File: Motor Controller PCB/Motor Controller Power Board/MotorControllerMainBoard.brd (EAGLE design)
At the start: 60 x 118 mm, 52 parts, among them U1 CDBA340L-G

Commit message: shrunk board size to 10x6cm
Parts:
- removed U$10, U$20: EEU-FM1H102B, MotorControllerEagleLibrary:EEU-FM1H102B
- C36, C37, C38, C39, C40: value (none) -> 22uF; device resistor:C1206 -> rcl:C1210
- moved C38 77.4 mm to (17.0, 35.5), flipped to the bottom
- moved C37 75.4 mm to (12.0, 37.0), flipped to the bottom, turned to 180 degrees
- moved C39 64.5 mm to (12.0, 49.0), flipped to the bottom, turned to 180 degrees
- moved C1 61.3 mm to (31.0, 74.0), turned to 0 degrees
- moved C36 48.1 mm to (12.0, 41.0), flipped to the bottom
- moved U$19 34.3 mm to (44.1, 40.0), flipped to the bottom, turned to 270 degrees
- moved U$18 31.8 mm to (53.0, 40.0), turned to 270 degrees
- moved U$13 31.1 mm to (35.3, 40.0), flipped to the top, turned to 270 degrees
- moved C40 24.2 mm to (12.0, 45.0), flipped to the bottom, turned to 180 degrees
- moved SV8 16.0 mm to (57.0, 26.7)
- moved C19 10.5 mm to (28.7, 44.1), flipped to the bottom
- moved SV9 10.3 mm to (48.3, 23.1), turned to 180 degrees
- moved U$22 9.43 mm to (40.0, 28.0)
- moved 3.3_CONFIRM 8.60 mm to (40.1, 30.1)
- moved L1 8.04 mm to (25.7, 39.4)
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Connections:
- net GND: no longer U$10.NEGATIVE, U$20.NEGATIVE
- net INPUT_POWER(+): no longer U$10.POSITIVE, U$20.POSITIVE
- net MOTOR_OUTPUT_(+): now also U$9.PIN4; no longer U$9.PIN5
- net POWER_INPUT(+): now also U$9.PIN5; no longer U$9.PIN4
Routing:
- net INPUT_POWER(+): track 0.00 -> 50.2 mm
- net 3.3V_ISOLATED: track 0.00 -> 35.8 mm
- net GND_ISOLATED: track 0.00 -> 29.3 mm, vias 0 -> 2
- net CURRENT_SENSOR_OUTPUT: track 0.00 -> 29.2 mm
- net N$17: track 0.00 -> 4.78 mm
- net GND: track 0.00 -> 3.66 mm
- net N$14: track 0.00 -> 2.27 mm
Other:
- board size 60 x 118 mm -> 60 x 100 mm

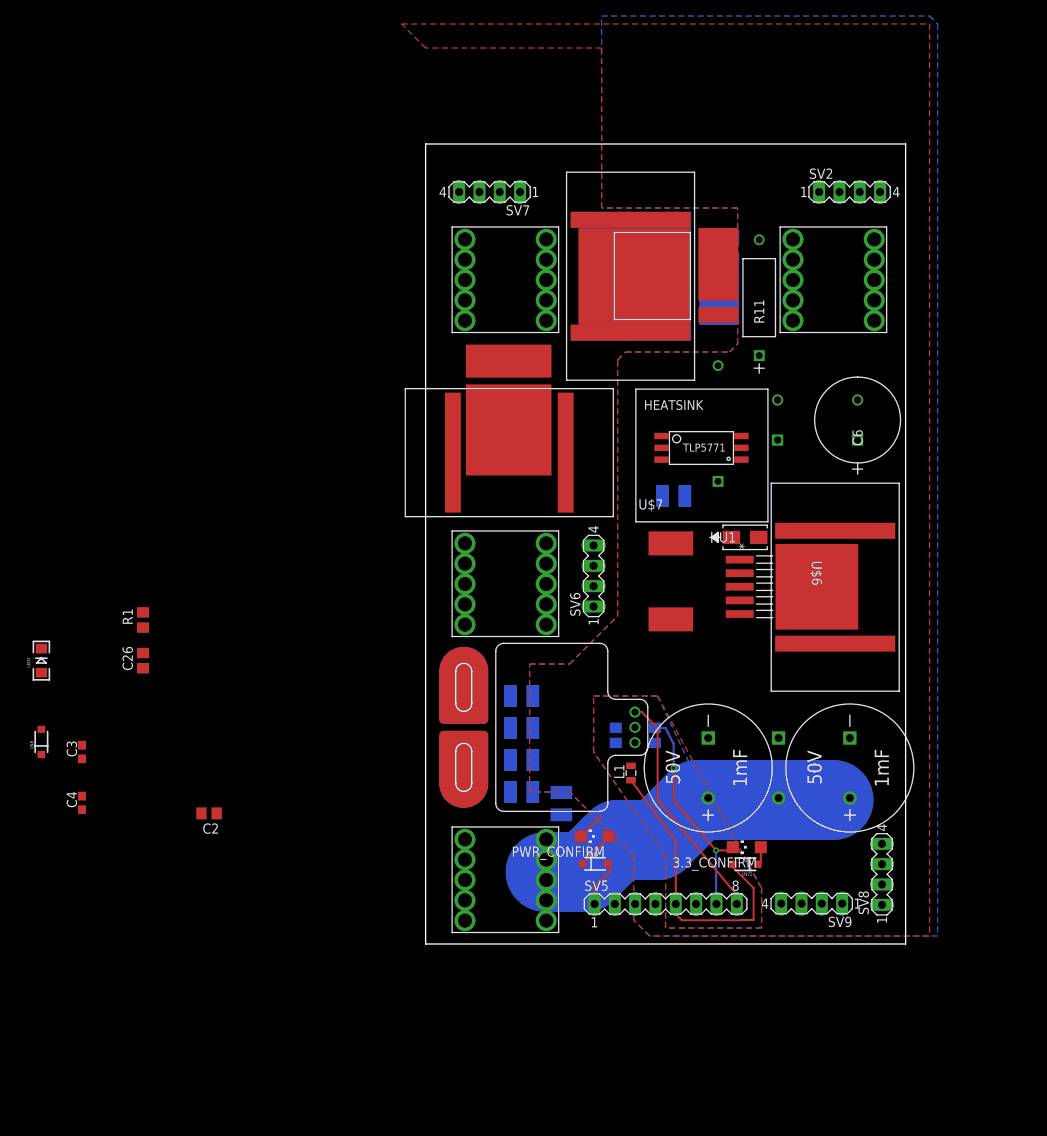
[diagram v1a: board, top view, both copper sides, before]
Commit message: Changed connections to logic board
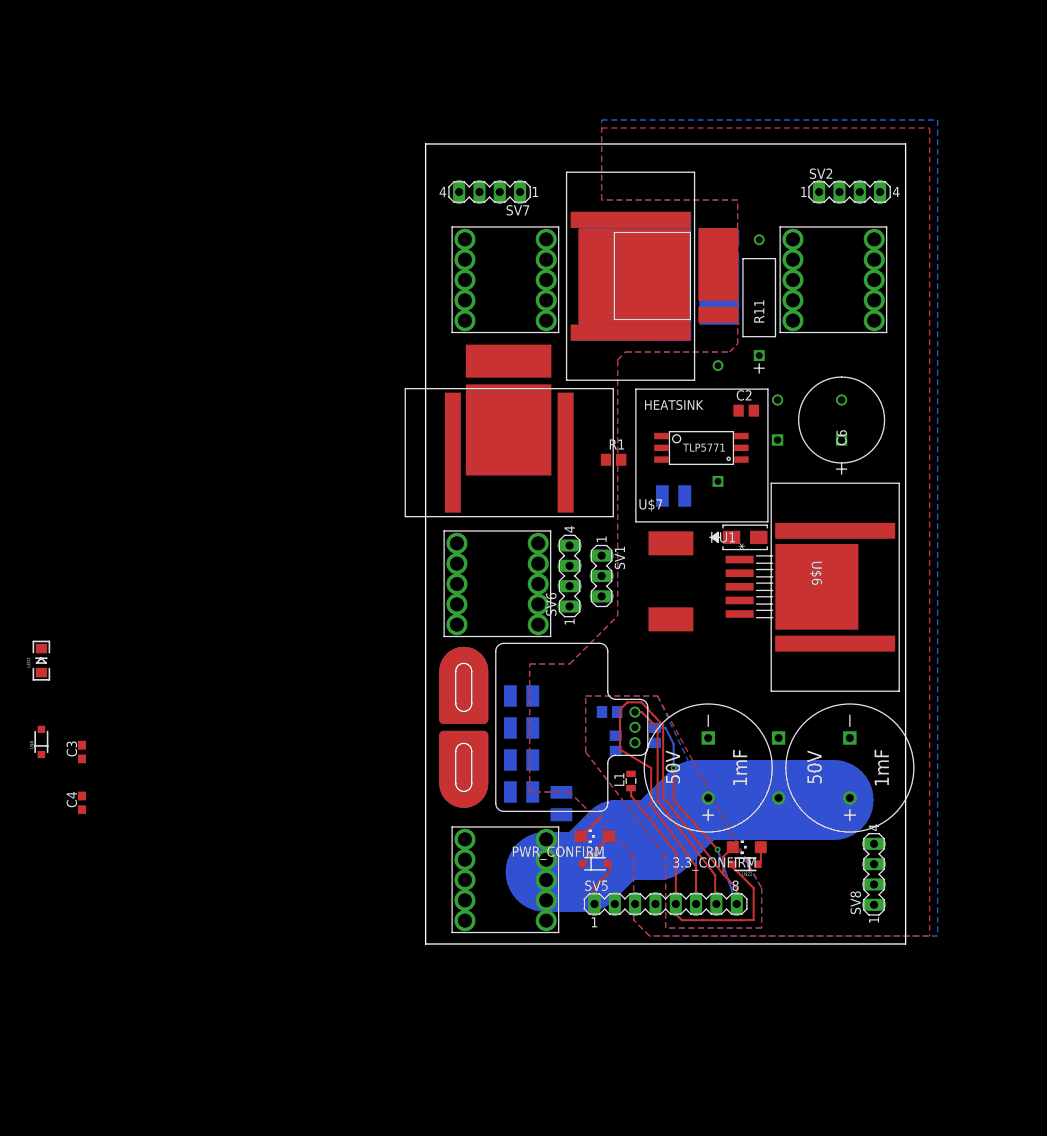
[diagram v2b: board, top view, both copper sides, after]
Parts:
- removed SV9: (no value), con-lstb:MA04-1
- added SV1: (no value), con-lstb:MA03-1
- moved C2 83.9 mm to (40.1, 84.7), turned to 0 degrees
- moved R1 62.1 mm to (23.5, 78.5), turned to 0 degrees
- moved C26 58.7 mm to (23.0, 47.0), flipped to the bottom, turned to 0 degrees
- moved SV6 3.00 mm to (18.0, 64.0)
- moved C6 2.00 mm to (52.0, 86.0)
- moved C20 1.00 mm to (23.8, 43.1)
- moved L1 1.00 mm to (25.7, 38.4)
- moved SV8 1.00 mm to (56.0, 26.7)
- moved U$15 1.00 mm to (9.00, 63.0)
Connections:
- net 3.3V_ISOLATED: now also SV1.1, SV6.1; no longer SV9.1
- net CURRENT_SENSOR_OUTPUT: now also SV5.7; no longer SV5.8, SV9.3
- net GND_ISOLATED: now also SV1.3, SV5.6, SV5.8, SV6.2, SV6.4; no longer SV5.7, SV9.4
- net TEENSY_FET_DRIVER_SIGNAL: now also SV1.2, SV6.3; no longer SV5.6, SV9.2
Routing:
- net GND_ISOLATED: track 29.3 -> 103.3 mm
- net INPUT_POWER(+): track 50.2 -> 54.8 mm
- net CURRENT_SENSOR_OUTPUT: track 29.2 -> 28.2 mm
- net 3.3V_ISOLATED: track 35.8 -> 34.9 mm

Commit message: this is going to be nuked when i change headers
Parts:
- added SV3: (no value), con-lstb:MA04-1
- added U$10: EEU-FM1H102B, MotorControllerEagleLibrary:EEU-FM1H102B
- moved U$11 53.6 mm to (73.2, 15.0)
- moved PWR_CONFIRM 53.4 mm to (73.2, 19.4)
- moved SV8 46.5 mm to (51.4, 73.0), turned to 0 degrees
- moved 3.3_CONFIRM 33.1 mm to (69.2, 14.1)
- moved U$13 32.9 mm to (24.3, 9.00)
- moved U$18 32.9 mm to (42.0, 9.00)
- moved U$19 32.9 mm to (33.1, 9.00)
- moved U$22 32.8 mm to (68.0, 11.0)
- moved U$12 18.0 mm to (9.00, 8.00)
- moved U$25 18.0 mm to (25.3, 52.8)
- moved U$17 18.0 mm to (38.6, 60.1)
- moved C1 18.0 mm to (31.0, 56.0)
- moved C19 18.0 mm to (28.7, 26.1)
- moved C2 18.0 mm to (40.1, 66.7)
- moved C20 18.0 mm to (23.8, 25.1)
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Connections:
- net GND: now also U$10.NEGATIVE
- net INPUT_POWER(+): now also U$10.POSITIVE
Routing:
- net GND_ISOLATED: track 103.3 -> 0.00 mm, vias 2 -> 0
- net INPUT_POWER(+): track 54.8 -> 0.00 mm
- net 3.3V_ISOLATED: track 34.9 -> 0.00 mm
- net CURRENT_SENSOR_OUTPUT: track 28.2 -> 0.00 mm
- net N$17: track 4.78 -> 0.00 mm
- net GND: track 3.66 -> 0.00 mm
- net N$14: track 2.27 -> 0.00 mm
- removed copper zone on layer 1, net N$3
- removed copper zone on layer 16, net N$5

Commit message: Made a layout, need labels
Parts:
- removed C5, C6: EEUFR1H221B, MotorControllerEagleLibrary:CAP_PAN_10X16
- removed SV2, SV3, SV6, SV7: (no value), con-lstb:MA04-1
- removed SV5: (no value), con-lstb:MA08-1
- removed U$24: DA-T263-101E, MotorControllerEagleLibrary:DA-T263-101E
- removed U$7: 100uH, MotorControllerEagleLibrary:INDUCTOR_SMD_FOOTPRINT
- removed U1: CDBA340L-G, MotorControllerEagleLibrary:CDBA-G
- added J1: (no value), SparkFun-Connectors:DB9
- 3.3_CONFIRM, PWR_CONFIRM: device led:CHIPLED_1206 -> SparkFun-LED:LED-1206
- U$12, U$14, U$15, U$16: value 732-3204-ND_CONNECTOR -> 74650073R; device Connector 732-3204:732-3204-ND -> MotorControllerEagleLibrary:74650073R
- U$6: value TL2575HV-15IKTTR -> KHHD004A2B; device MotorControllerEagleLibrary:KTT5_6P22X6P86 -> MotorControllerEagleLibrary:KHHD004A2B
- moved C4 108.9 mm to (60.0, 71.0), turned to 0 degrees
- moved C3 105.6 mm to (58.0, 73.1), turned to 0 degrees
- moved LED2 100.6 mm to (52.0, 43.0)
- moved U$8 97.0 mm to (49.0, 42.0)
- moved U$12 82.0 mm to (7.00, 90.0), turned to 0 degrees
- moved U$15 61.7 mm to (56.0, 85.0)
- moved U$16 60.1 mm to (6.00, 23.0), turned to 0 degrees
- moved U$14 53.3 mm to (5.00, 56.0), turned to 0 degrees
- moved U$11 45.1 mm to (37.0, 42.0), turned to 90 degrees
- moved PWR_CONFIRM 40.7 mm to (40.0, 43.0)
- moved U$22 39.9 mm to (43.0, 42.0), turned to 90 degrees
- moved 3.3_CONFIRM 37.0 mm to (46.0, 43.0)
- moved C38 32.7 mm to (49.0, 11.0), turned to 270 degrees
- moved U$6 32.0 mm to (21.0, 29.0), flipped to the bottom, turned to 90 degrees
- moved C40 31.4 mm to (39.0, 11.0), turned to 270 degrees
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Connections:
- removed net N$1: U$6.2, U$7.1, U1.1
- removed net POWER_INPUT(+): U$9.PIN5
- new net ENABLE_12V: J1.8, U$6.ON/OFF
- new net N$11: U$6.SENSE+
- new net N$5: U$6.SENSE-
- new net N$8: U$6.TRIM
- net 12V_POWER_REGULATED: now also J1.2, U$6.VO+; no longer C5.1, C6.1, U$6.4, U$7.2
- net 3.3V_ISOLATED: now also J1.1, J1.9; no longer SV5.5, SV6.1
- net CURRENT_SENSOR_OUTPUT: now also J1.5; no longer SV5.7
- net GND: now also J1.7, U$15.P$1, U$15.P$2, U$15.P$3, U$15.P$4, U$6.VI-, U$6.VO-; no longer C5.2, C6.2, SV5.3, SV5.4, U$14.P$1, U$14.P$10, U$14.P$2, U$14.P$3, U$14.P$4, U$14.P$5, U$14.P$6, U$14.P$7, U$14.P$8, U$14.P$9, U$24.GND, U$24.GND2\, U$6.3, U$6.5, U$6.6, U1.2
- net GND_ISOLATED: now also J1.4; no longer SV5.6, SV5.8, SV6.2, SV6.4
- net INPUT_POWER(+): now also J1.3, U$14.P$1, U$14.P$2, U$14.P$3, U$14.P$4, U$6.VI+, U$9.PIN4; no longer C36.1, C37.1, C38.1, C39.1, C40.1, SV5.1, SV5.2, U$10.POSITIVE, U$12.P$1, U$12.P$10, U$12.P$2, U$12.P$3, U$12.P$4, U$12.P$5, U$12.P$6, U$12.P$7, U$12.P$8, U$12.P$9, U$13.POSITIVE, U$18.POSITIVE, U$19.POSITIVE
- net MOTOR_OUTPUT_(+): now also C36.1, C37.1, C38.1, C39.1, C40.1, U$10.POSITIVE, U$13.POSITIVE, U$16.P$1, U$16.P$2, U$16.P$3, U$16.P$4, U$18.POSITIVE, U$19.POSITIVE, U$9.PIN5; no longer U$15.P$1, U$15.P$10, U$15.P$2, U$15.P$3, U$15.P$4, U$15.P$5, U$15.P$6, U$15.P$7, U$15.P$8, U$15.P$9, U$6.1, U$9.PIN4
- net MOTOR_OUTPUT_(--): now also U$12.P$1, U$12.P$2, U$12.P$3, U$12.P$4; no longer U$16.P$1, U$16.P$10, U$16.P$2, U$16.P$3, U$16.P$4, U$16.P$5, U$16.P$6, U$16.P$7, U$16.P$8, U$16.P$9
- net TEENSY_FET_DRIVER_SIGNAL: now also J1.6, U$17.1.ANODE; no longer SV6.3
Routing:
- net INPUT_POWER(+): track 0.00 -> 131.8 mm, vias 0 -> 2
- net 12V_POWER_REGULATED: track 0.00 -> 103.0 mm, vias 0 -> 2
- net GND_ISOLATED: track 0.00 -> 97.9 mm, vias 0 -> 1
- net MOTOR_OUTPUT_(+): track 0.00 -> 72.1 mm
- net 3.3V_ISOLATED: track 0.00 -> 62.4 mm, vias 0 -> 2
- net GND: track 0.00 -> 56.9 mm, vias 0 -> 22
- net ENABLE_12V: track 0.00 -> 55.5 mm
- net FET_DRIVER_SIGNAL: track 0.00 -> 50.3 mm
- net CURRENT_SENSOR_OUTPUT: track 0.00 -> 39.4 mm
- net TEENSY_FET_DRIVER_SIGNAL: track 0.00 -> 35.8 mm
- net N$10: track 0.00 -> 17.4 mm
- net N$7: track 0.00 -> 12.8 mm
- net N$2: track 0.00 -> 9.98 mm
- net N$6: track 0.00 -> 8.52 mm
- net N$14: track 0.00 -> 3.47 mm
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- added copper zone on layer 1, net INPUT_POWER(+)
- added copper zone on layer 16, net INPUT_POWER(+)
- added copper zone on layer 1, net MOTOR_OUTPUT_(+)
- added copper zone on layer 16, net MOTOR_OUTPUT_(+)
- added copper zone on layer 1, net MOTOR_OUTPUT_(--)
- added copper zone on layer 16, net MOTOR_OUTPUT_(--)
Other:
- board size 60 x 100 mm -> 70 x 100 mm

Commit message: added TVS diodes and text
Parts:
- removed SV8: (no value), con-lstb:MA04-1
- added SV2: (no value), con-lstb:MA03-1
- added U$20, U$7: SMBJ15CD, MotorControllerEagleLibrary:SMB-DIODE
- added U$21, U$24: SS110-TP, MotorControllerEagleLibrary:SMA-DIODE
- moved U$12 7.00 mm to (14.0, 90.0)
- moved U$16 1.41 mm to (5.00, 24.0)
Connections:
- new net N$1: U$24.A, U$7.A
- new net N$4: U$20.A, U$21.A
- net 12V_POWER_REGULATED: now also SV2.1; no longer SV8.2
- net FET_DRIVER_SIGNAL: now also SV2.2; no longer SV8.3
- net GND: now also SV2.3, U$21.C, U$24.C; no longer SV8.4
- net MOTOR_OUTPUT_(+): no longer SV8.1
- net N$10: now also U$20.C
- net N$2: now also U$7.C
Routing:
- net MOTOR_OUTPUT_(+): track 72.1 -> 0.00 mm
- net 3.3V_ISOLATED: track 62.4 -> 78.8 mm, vias 2 -> 3
- net N$10: track 17.4 -> 23.9 mm
- net N$4: track 0.00 -> 5.69 mm
- net N$2: track 9.98 -> 15.6 mm
- net N$1: track 0.00 -> 4.18 mm
- net INPUT_POWER(+): track 131.8 -> 132.5 mm
- net GND: vias 22 -> 21
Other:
- board text added: "12V"
- board text added: "12V_ON"
- board text added: "3.3V_ISO"
- board text added: "3.3V_ON"
- board text added: "DRVR_SIG"
- board text added: "GND"
- board text added: "GND_ISO"
- board text added: "M+"
- board text added: "M-"
- board text added: "PWR_ON"
- board text added: "TNZY_FET_DRVR"
- board text removed: "Logic Board"

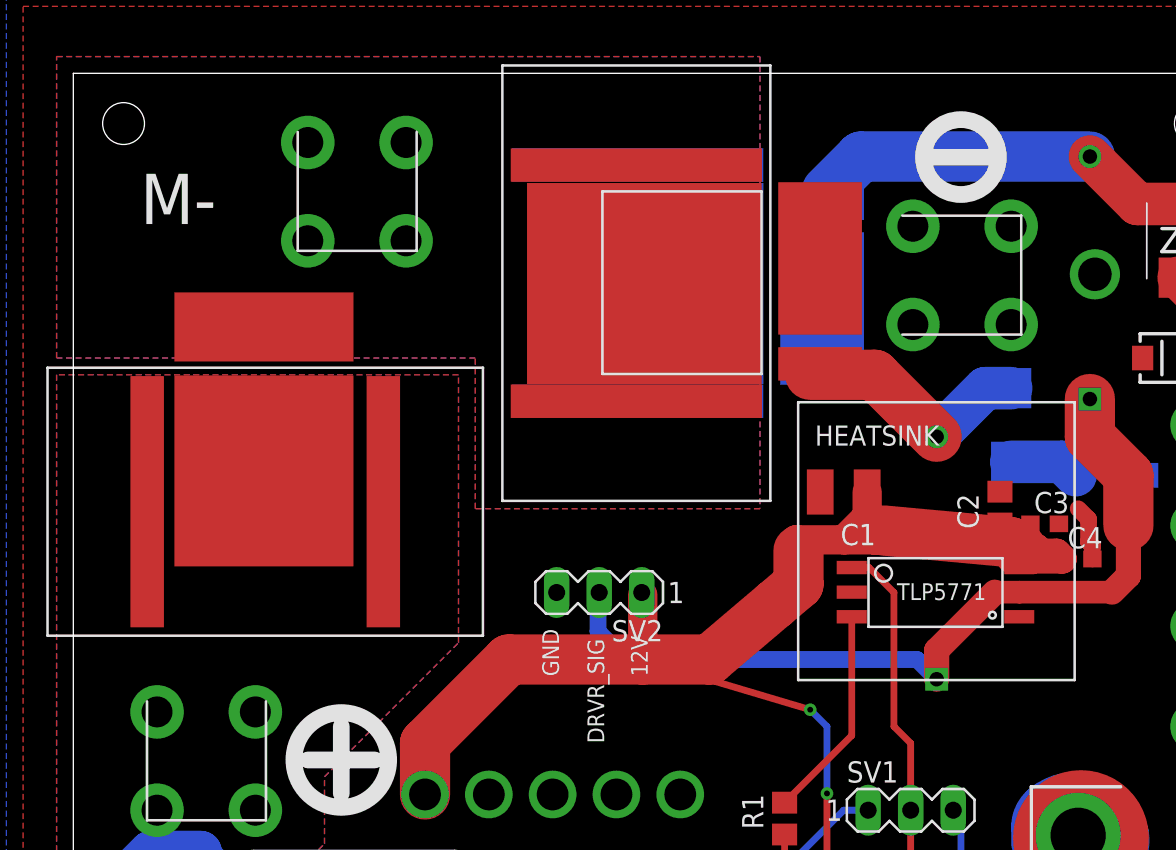
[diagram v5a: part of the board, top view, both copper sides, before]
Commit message: Added via for thermals
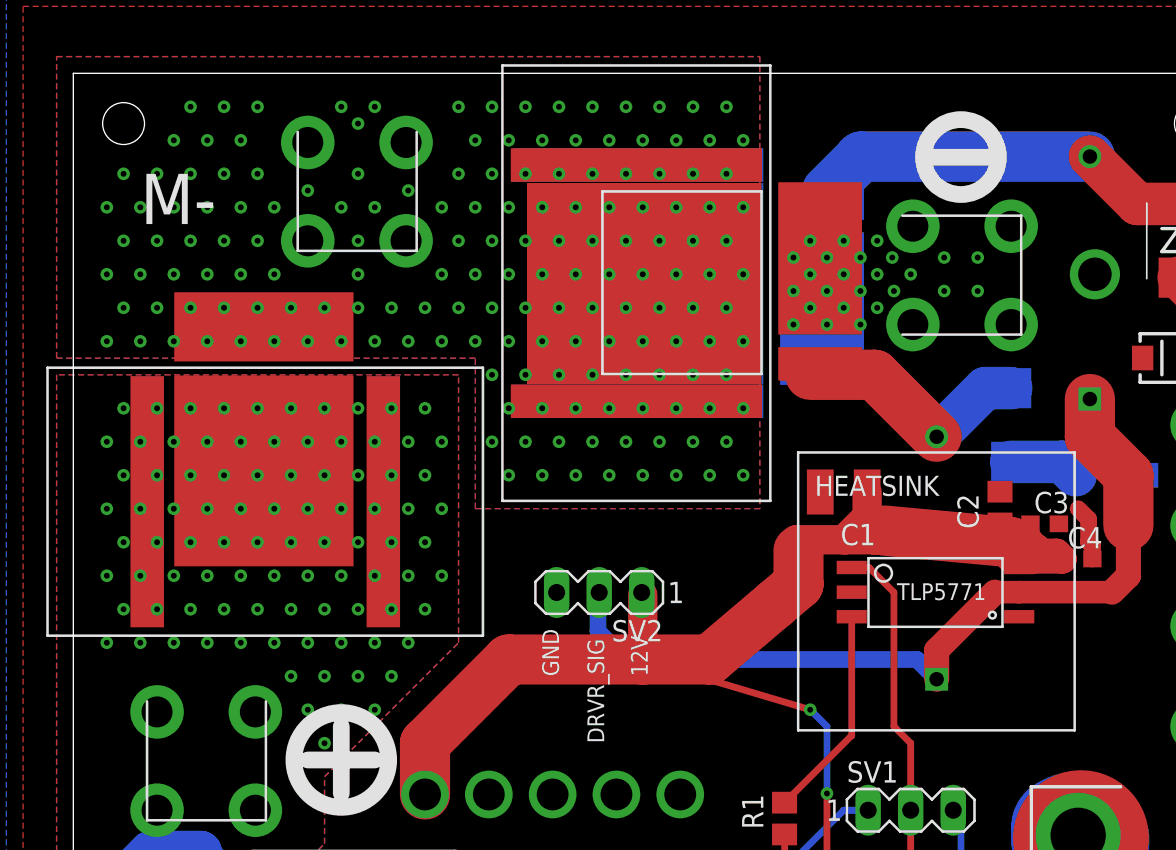
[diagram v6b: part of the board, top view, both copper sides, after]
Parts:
- moved U$25 3.00 mm to (43.3, 60.8)
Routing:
- net INPUT_POWER(+): vias 2 -> 93
- net GND: vias 21 -> 46
